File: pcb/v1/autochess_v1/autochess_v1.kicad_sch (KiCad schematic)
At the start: 3 parts, among them J1 Raspberry_Pi_2_3, U1 ATmega328P-P

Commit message: Make some progress on the PCB
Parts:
- added C65: 100uF, symbol Device:C
- added C66: 0.1uF, symbol Device:C
- added D65: 3A, symbol Device:D
- added F1: Polyfuse, symbol Device:Polyfuse
- added J2: POWER_IN, symbol Connector:Barrel_Jack
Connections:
- net GND: now also J1.14 (GND), J1.20 (GND), J1.25 (GND), J1.30 (GND), J1.34 (GND), J1.39 (GND), J1.6 (GND), J1.9 (GND), C65.2, C66.2, D65.2 (A), J2.2
- net VCC: now also J1.2 (5V), J1.4 (5V), C65.1, C66.1, D65.1 (K), F1.2
- net sensors/SENSOR_OUT_8: now reaches U1.1 (~{RESET}/PC6)
- net sensors/SENSOR_ON_6: now reaches U1.11 (PD5)
- net sensors/SENSOR_ON_7: now reaches U1.12 (PD6)
- net sensors/SENSOR_ON_8: now reaches U1.13 (PD7)
- net sensors/SENSOR_ON_1: now reaches U1.2 (PD0)
- net sensors/SENSOR_OUT_1: now reaches U1.23 (PC0)
- net sensors/SENSOR_OUT_2: now reaches U1.24 (PC1)
- net sensors/SENSOR_OUT_3: now reaches U1.25 (PC2)
- net sensors/SENSOR_OUT_4: now reaches U1.26 (PC3)
- net sensors/SENSOR_OUT_5: now reaches U1.27 (PC4)
- net sensors/SENSOR_OUT_6: now reaches U1.28 (PC5)
- net sensors/SENSOR_ON_2: now reaches U1.3 (PD1)
- net sensors/SENSOR_ON_3: now reaches U1.4 (PD2)
- net sensors/SENSOR_ON_4: now reaches U1.5 (PD3)
- net sensors/SENSOR_ON_5: now reaches U1.6 (PD4)
- new net: F1.1, J2.1
- no-connect marks 0 -> 4
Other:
- added sheet sensors (sensors.kicad_sch)
- note added: "TODO: Calculate fuse and TVS diode values"
- moved on the sheet: J1, R1, U1

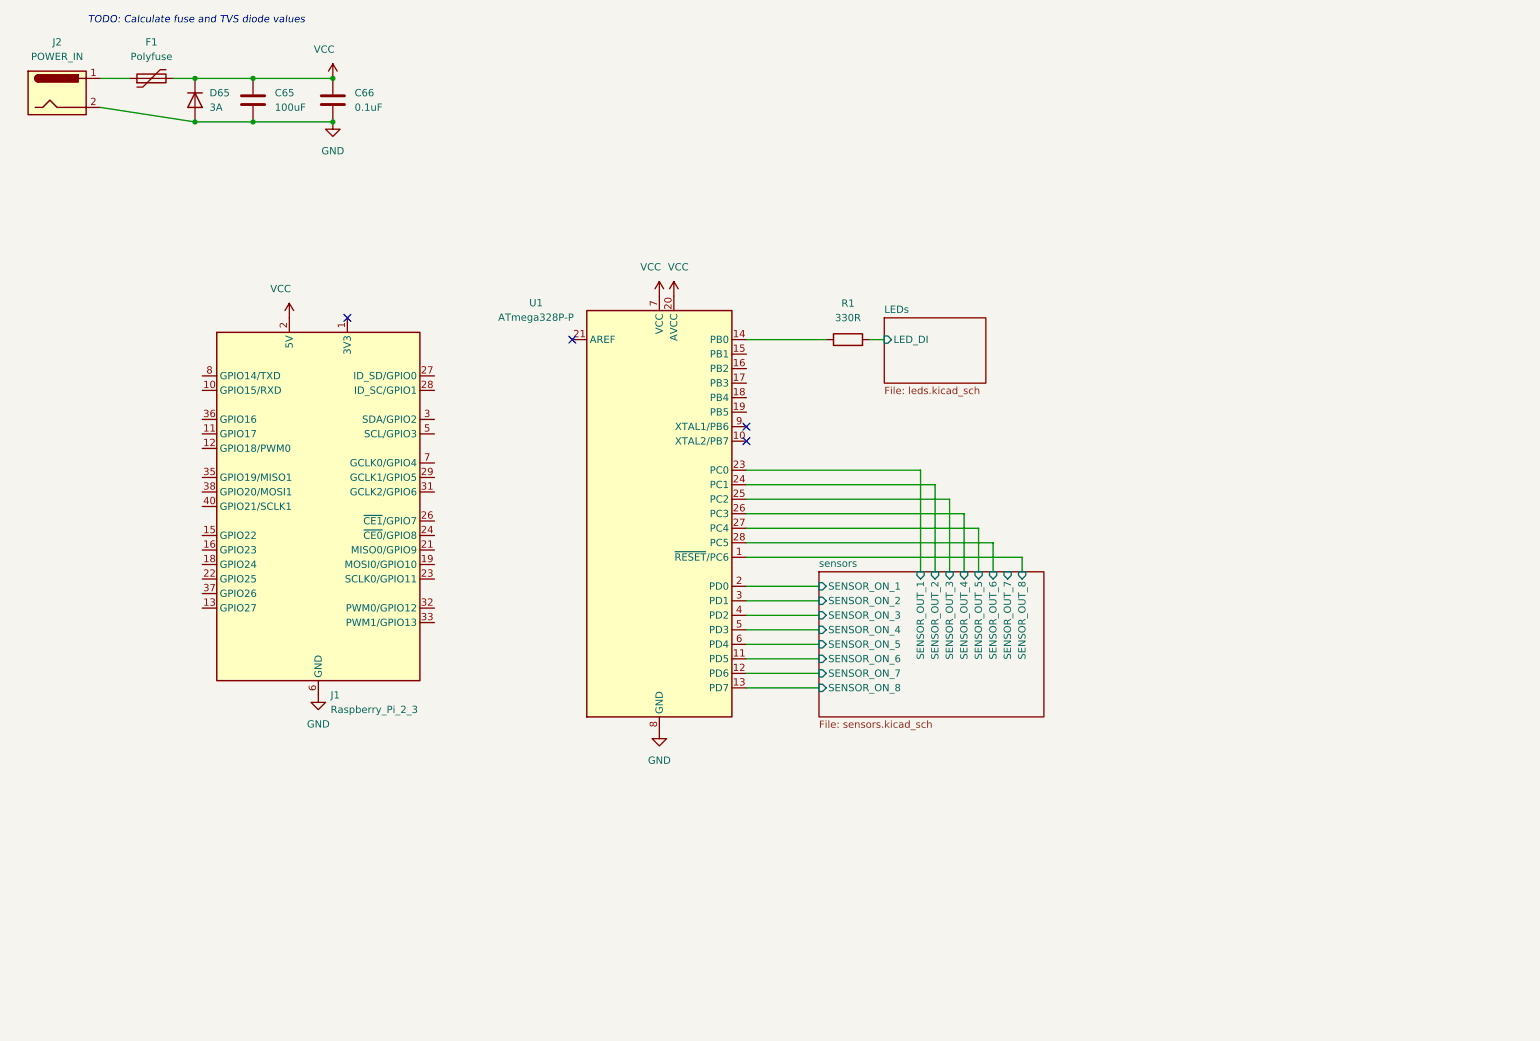
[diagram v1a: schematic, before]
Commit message: Finish the schematic draft, start pcb layout
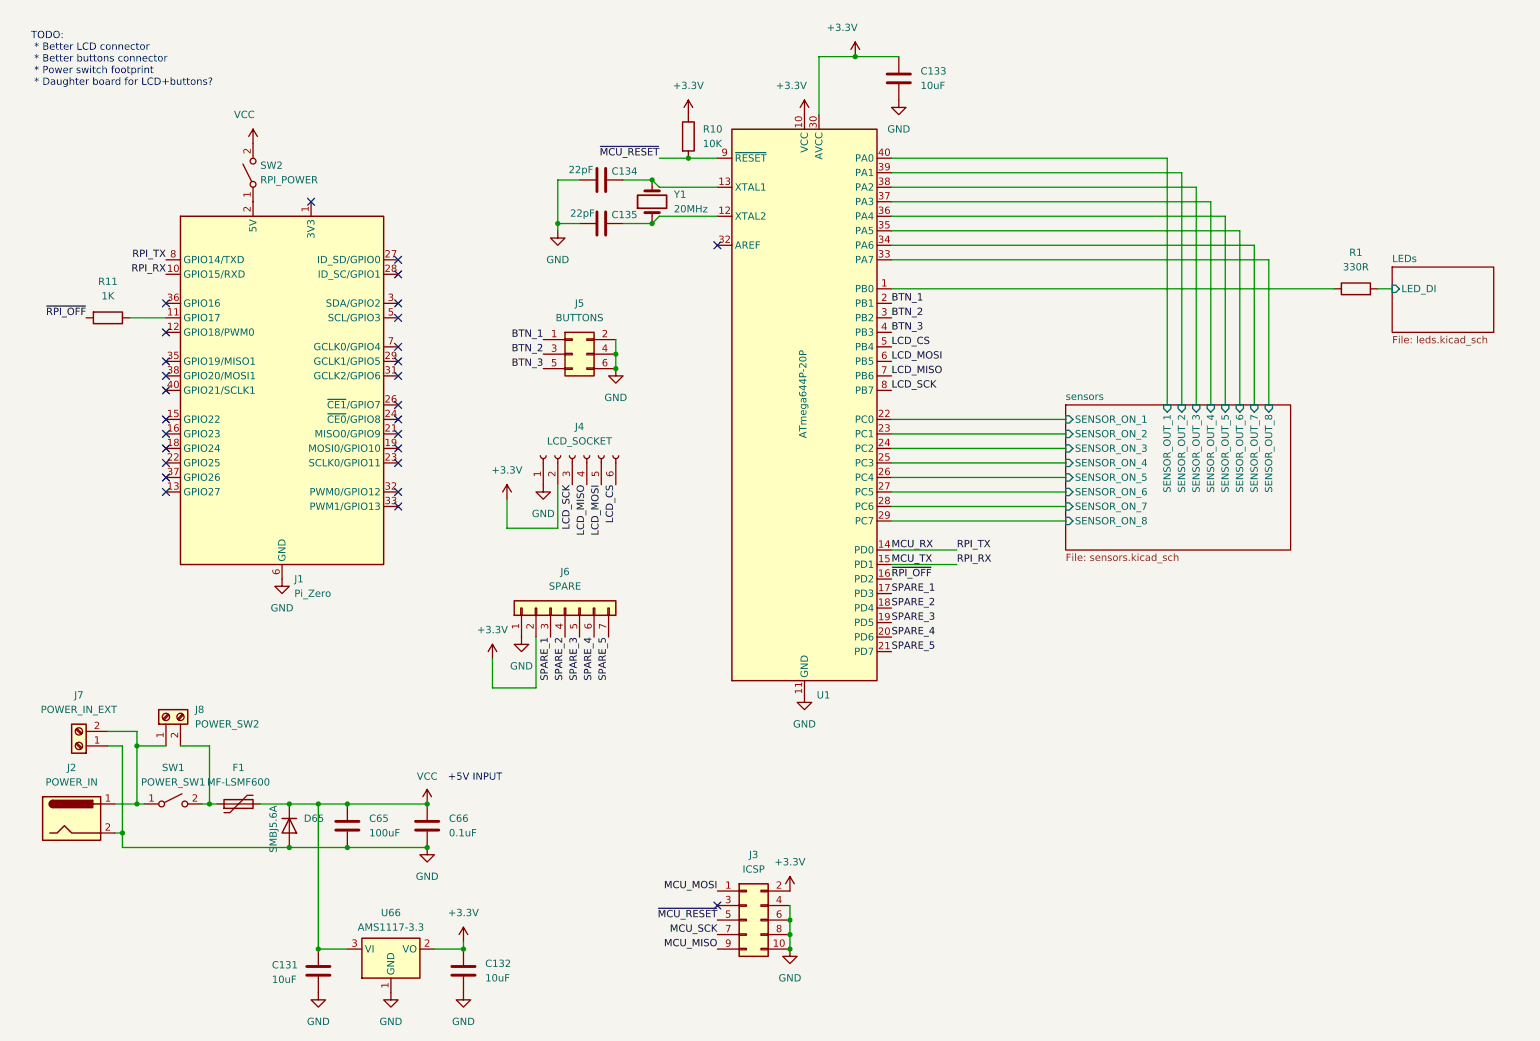
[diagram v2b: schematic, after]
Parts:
- removed U1: ATmega328P-P, Package_DIP:DIP-28_W7.62mm, symbol MCU_Microchip_ATmega:ATmega328P-P
- added C131, C132, C133: 10uF, Capacitor_SMD:C_1206_3216Metric_Pad1.33x1.80mm_HandSolder, symbol Device:C
- added C134, C135: 22pF, Capacitor_SMD:C_1206_3216Metric_Pad1.33x1.80mm_HandSolder, symbol Device:C
- added J3: ICSP, Connector_IDC:IDC-Header_2x05_P2.54mm_Horizontal, symbol Connector_Generic:Conn_02x05_Odd_Even
- added J4: LCD_SOCKET, Connector_PinHeader_2.54mm:PinHeader_1x06_P2.54mm_Vertical, symbol Connector:Conn_01x06_Socket
- added J5: BUTTONS, Connector_PinHeader_2.54mm:PinHeader_2x03_P2.54mm_Vertical, symbol Connector_Generic:Conn_02x03_Odd_Even
- added J6: SPARE, Connector_PinHeader_2.54mm:PinHeader_1x07_P2.54mm_Vertical, symbol Connector_Generic:Conn_01x07
- added J7: POWER_IN_EXT, TerminalBlock_Altech:Altech_AK100_1x02_P5.00mm, symbol Connector:Screw_Terminal_01x02
- added J8: POWER_SW2, TerminalBlock_Altech:Altech_AK100_1x02_P5.00mm, symbol Connector:Screw_Terminal_01x02
- added R10: 10K, Resistor_SMD:R_1206_3216Metric_Pad1.30x1.75mm_HandSolder, symbol Device:R
- added R11: 1K, Resistor_SMD:R_1206_3216Metric_Pad1.30x1.75mm_HandSolder, symbol Device:R
- added SW1: POWER_SW1, Autochess:Marquardt_1858_4205, symbol Switch:SW_SPST
- added SW2: RPI_POWER, Jumper:SolderJumper-2_P1.3mm_Open_TrianglePad1.0x1.5mm, symbol Switch:SW_SPST
- added U1: ATmega644P-20P, Package_DIP:DIP-40_W15.24mm, symbol MCU_Microchip_ATmega:ATmega644P-20P
- added U66: AMS1117-3.3, Package_TO_SOT_SMD:SOT-223-3_TabPin2, symbol Regulator_Linear:AMS1117-3.3
- added Y1: 20MHz, Crystal:Crystal_HC49-U_Vertical, symbol Device:Crystal
- C65, C66: footprint (none) -> Capacitor_SMD:C_1206_3216Metric_Pad1.33x1.80mm_HandSolder
- D65: value 3A -> SMBJ5.6A; footprint (none) -> Diode_SMD:D_SMB_Handsoldering
- F1: value Polyfuse -> MF-LSMF600; footprint (none) -> Fuse:Fuse_2920_7451Metric_Pad2.10x5.45mm_HandSolder
- J1: value Raspberry_Pi_2_3 -> Pi_Zero; footprint (none) -> Connector_PinHeader_2.54mm:PinHeader_2x20_P2.54mm_Vertical
- J2: footprint (none) -> Connector_BarrelJack:BarrelJack_Horizontal
- R1: footprint (none) -> Resistor_SMD:R_1206_3216Metric_Pad1.30x1.75mm_HandSolder
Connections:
- net GND: now also C131.2, C132.2, C133.2, C134.2, C135.2, J3.10 (Pin_10), J3.4 (Pin_4), J3.6 (Pin_6), J3.8 (Pin_8), J4.1 (Pin_1), J5.2 (Pin_2), J5.4 (Pin_4), J5.6 (Pin_6), J6.1 (Pin_1), J7.1 (Pin_1), U1.11 (GND), U1.31 (GND), U66.1 (GND)
- net VCC: now also C131.1, SW2.2 (B), U66.3 (VI); no longer J1.2 (5V), J1.4 (5V)
- net sensors/SENSOR_ON_1: now also U1.22 (PC0)
- net sensors/SENSOR_ON_2: now also U1.23 (PC1)
- net sensors/SENSOR_ON_3: now also U1.24 (PC2)
- net sensors/SENSOR_ON_4: now also U1.25 (PC3)
- net sensors/SENSOR_ON_5: now also U1.26 (PC4)
- net sensors/SENSOR_ON_6: now also U1.27 (PC5)
- net sensors/SENSOR_ON_7: now also U1.28 (PC6)
- net sensors/SENSOR_ON_8: now also U1.29 (PC7)
- net sensors/SENSOR_OUT_1: now also U1.40 (PA0)
- net sensors/SENSOR_OUT_2: now also U1.39 (PA1)
- net sensors/SENSOR_OUT_3: now also U1.38 (PA2)
- net sensors/SENSOR_OUT_4: now also U1.37 (PA3)
- net sensors/SENSOR_OUT_5: now also U1.36 (PA4)
- net sensors/SENSOR_OUT_6: now also U1.35 (PA5)
- net sensors/SENSOR_OUT_7: now also U1.34 (PA6)
- net sensors/SENSOR_OUT_8: now also U1.33 (PA7)
- net MCU_TX: now reaches J1.10 (GPIO15/RXD)
- net MCU_TX: now also U1.15 (PD1)
- net at J1.11 (GPIO17): now also R11.1
- net MCU_RX: now reaches J1.8 (GPIO14/TXD)
- net MCU_RX: now also U1.14 (PD0)
- net at R1.1: now also U1.1 (PB0)
- net at J2.1: now also J7.2 (Pin_2), J8.1 (Pin_1), SW1.1 (A); no longer F1.1
- new net: J1.2 (5V), J1.4 (5V), SW2.1 (A)
- new net: F1.1, J8.2 (Pin_2), SW1.2 (B)
- new net: C135.1, U1.12 (XTAL2), Y1.1
- new net: C134.1, U1.13 (XTAL1), Y1.2
- new net +3.3V: C132.1, C133.1, J3.2 (Pin_2), J4.2 (Pin_2), J6.2 (Pin_2), R10.1, U1.10 (VCC), U1.30 (AVCC), U66.2 (VO)
- new net BTN_1: J5.1 (Pin_1), U1.2 (PB1)
- new net BTN_2: J5.3 (Pin_3), U1.3 (PB2)
- new net BTN_3: J5.5 (Pin_5), U1.4 (PB3)
- new net LCD_CS: J4.6 (Pin_6), U1.5 (PB4)
- new net LCD_MISO: J4.4 (Pin_4), U1.7 (PB6)
- new net LCD_MOSI: J4.5 (Pin_5), U1.6 (PB5)
- new net LCD_SCK: J4.3 (Pin_3), U1.8 (PB7)
- new net MCU_MISO: J3.9 (Pin_9)
- new net MCU_MOSI: J3.1 (Pin_1)
- new net MCU_SCK: J3.7 (Pin_7)
- new net SPARE_1: J6.3 (Pin_3), U1.17 (PD3)
- new net SPARE_2: J6.4 (Pin_4), U1.18 (PD4)
- new net SPARE_3: J6.5 (Pin_5), U1.19 (PD5)
- new net SPARE_4: J6.6 (Pin_6), U1.20 (PD6)
- new net SPARE_5: J6.7 (Pin_7), U1.21 (PD7)
- new net ~{MCU_RESET}: J3.5 (Pin_5), R10.2, U1.9 (~{RESET})
- new net ~{RPI_OFF}: R11.2, U1.16 (PD2)
- no-connect marks 4 -> 28
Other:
- note added: "+5V INPUT"
- note added: "TODO: * Better LCD connector * Better buttons connector * Power switch footprint * Daughter board for LCD+buttons?"
- note removed: "TODO: Calculate fuse and TVS diode values"
- moved on the sheet: C65, C66, D65, F1, J1, J2, R1

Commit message: Continue laying out the PCB
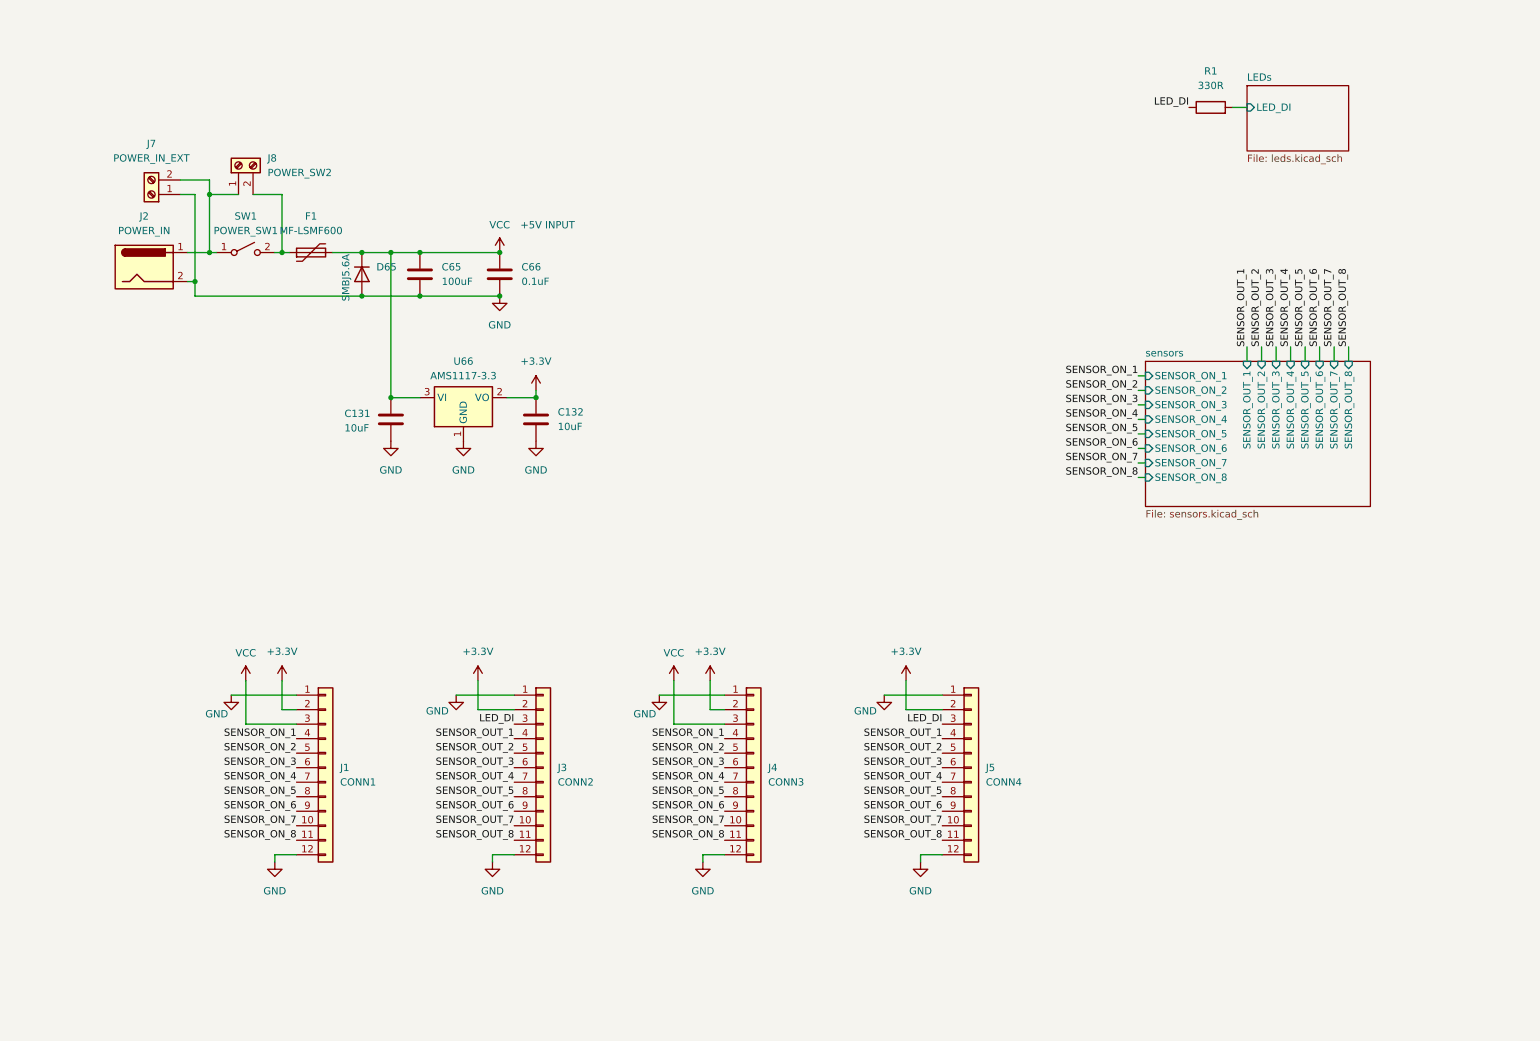
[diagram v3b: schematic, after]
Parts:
- removed C133: 10uF, Capacitor_SMD:C_1206_3216Metric_Pad1.33x1.80mm_HandSolder, symbol Device:C
- removed C134, C135: 22pF, Capacitor_SMD:C_1206_3216Metric_Pad1.33x1.80mm_HandSolder, symbol Device:C
- removed J1: Pi_Zero, Connector_PinHeader_2.54mm:PinHeader_2x20_P2.54mm_Vertical, symbol Connector:Raspberry_Pi_2_3
- removed J3: ICSP, Connector_IDC:IDC-Header_2x05_P2.54mm_Horizontal, symbol Connector_Generic:Conn_02x05_Odd_Even
- removed J4: LCD_SOCKET, Connector_PinHeader_2.54mm:PinHeader_1x06_P2.54mm_Vertical, symbol Connector:Conn_01x06_Socket
- removed J5: BUTTONS, Connector_PinHeader_2.54mm:PinHeader_2x03_P2.54mm_Vertical, symbol Connector_Generic:Conn_02x03_Odd_Even
- removed J6: SPARE, Connector_PinHeader_2.54mm:PinHeader_1x07_P2.54mm_Vertical, symbol Connector_Generic:Conn_01x07
- removed R10: 10K, Resistor_SMD:R_1206_3216Metric_Pad1.30x1.75mm_HandSolder, symbol Device:R
- removed R11: 1K, Resistor_SMD:R_1206_3216Metric_Pad1.30x1.75mm_HandSolder, symbol Device:R
- removed SW2: RPI_POWER, Jumper:SolderJumper-2_P1.3mm_Open_TrianglePad1.0x1.5mm, symbol Switch:SW_SPST
- removed U1: ATmega644P-20P, Package_DIP:DIP-40_W15.24mm, symbol MCU_Microchip_ATmega:ATmega644P-20P
- removed Y1: 20MHz, Crystal:Crystal_HC49-U_Vertical, symbol Device:Crystal
- added J1: CONN1, Connector_PinHeader_2.54mm:PinHeader_1x12_P2.54mm_Vertical, symbol Connector_Generic:Conn_01x12
- added J3: CONN2, Connector_PinHeader_2.54mm:PinHeader_1x12_P2.54mm_Vertical, symbol Connector_Generic:Conn_01x12
- added J4: CONN3, Connector_PinHeader_2.54mm:PinHeader_1x12_P2.54mm_Vertical, symbol Connector_Generic:Conn_01x12
- added J5: CONN4, Connector_PinHeader_2.54mm:PinHeader_1x12_P2.54mm_Vertical, symbol Connector_Generic:Conn_01x12
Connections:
- net +3.3V: now also J1.2 (Pin_2), J3.2 (Pin_2), J4.2 (Pin_2), J5.2 (Pin_2)
- net GND: now also J1.1 (Pin_1), J1.12 (Pin_12), J3.1 (Pin_1), J3.12 (Pin_12), J4.1 (Pin_1), J4.12 (Pin_12), J5.1 (Pin_1), J5.12 (Pin_12)
- net VCC: now also J1.3 (Pin_3), J4.3 (Pin_3)
- net LED_DI: now reaches R1.1
- net LED_DI: now also J3.3 (Pin_3), J5.3 (Pin_3)
- new net SENSOR_ON_1: J1.4 (Pin_4), J4.4 (Pin_4)
- new net SENSOR_ON_2: J1.5 (Pin_5), J4.5 (Pin_5)
- new net SENSOR_ON_3: J1.6 (Pin_6), J4.6 (Pin_6)
- new net SENSOR_ON_4: J1.7 (Pin_7), J4.7 (Pin_7)
- new net SENSOR_ON_5: J1.8 (Pin_8), J4.8 (Pin_8)
- new net SENSOR_ON_6: J1.9 (Pin_9), J4.9 (Pin_9)
- new net SENSOR_ON_7: J1.10 (Pin_10), J4.10 (Pin_10)
- new net SENSOR_ON_8: J1.11 (Pin_11), J4.11 (Pin_11)
- new net SENSOR_OUT_1: J3.4 (Pin_4), J5.4 (Pin_4)
- new net SENSOR_OUT_2: J3.5 (Pin_5), J5.5 (Pin_5)
- new net SENSOR_OUT_3: J3.6 (Pin_6), J5.6 (Pin_6)
- new net SENSOR_OUT_4: J3.7 (Pin_7), J5.7 (Pin_7)
- new net SENSOR_OUT_5: J3.8 (Pin_8), J5.8 (Pin_8)
- new net SENSOR_OUT_6: J3.9 (Pin_9), J5.9 (Pin_9)
- new net SENSOR_OUT_7: J3.10 (Pin_10), J5.10 (Pin_10)
- new net SENSOR_OUT_8: J3.11 (Pin_11), J5.11 (Pin_11)
- no-connect marks 28 -> 0
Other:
- note removed: "TODO: * Better LCD connector * Better buttons connector * Power switch footprint * Daughter board for LCD+buttons?"
- moved on the sheet: C131, C132, C65, C66, D65, F1, J2, J7, J8, R1, SW1, U66

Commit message: Continue placing
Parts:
- renumbered C65 to C133, C66 to C134
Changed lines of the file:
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@@
 		(dnp no)
 		(fields_autoplaced yes)
-		(property "Reference" "C66"
+		(property "Reference" "C134"
 			(at 102.87 59.6899 0)
 			(show_name no)
@@
 			(project "autochess_v1"
 				(path "/3df8ff08-9f77-4f65-9fed-81b599c9e86e"
-					(reference "C66")
+					(reference "C134")
 					(unit 1)
 				)
@@
 		(dnp no)
 		(fields_autoplaced yes)
-		(property "Reference" "C65"
+		(property "Reference" "C133"
 			(at 88.9 59.6899 0)
 			(show_name no)
@@
 			(project "autochess_v1"
 				(path "/3df8ff08-9f77-4f65-9fed-81b599c9e86e"
-					(reference "C65")
+					(reference "C133")
 					(unit 1)
 				)

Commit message: Place most components
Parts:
- renumbered J3 to J2, J4 to J3, J5 to J4, J2 to J9
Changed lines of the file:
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@@
 		(dnp no)
 		(fields_autoplaced yes)
-		(property "Reference" "J3"
+		(property "Reference" "J2"
 			(at 109.22 147.3199 0)
 			(show_name no)
@@
 			(project "autochess_v1"
 				(path "/3df8ff08-9f77-4f65-9fed-81b599c9e86e"
-					(reference "J3")
+					(reference "J2")
 					(unit 1)
 				)
@@
 		(dnp no)
 		(fields_autoplaced yes)
-		(property "Reference" "J2"
+		(property "Reference" "J9"
 			(at 36.83 50.8 0)
 			(show_name no)
@@
 			(project "autochess_v1"
 				(path "/3df8ff08-9f77-4f65-9fed-81b599c9e86e"
-					(reference "J2")
+					(reference "J9")
 					(unit 1)
 				)
@@
 		(dnp no)
 		(fields_autoplaced yes)
-		(property "Reference" "J5"
+		(property "Reference" "J4"
 			(at 184.15 147.3199 0)
 			(show_name no)
@@
 			(project "autochess_v1"
 				(path "/3df8ff08-9f77-4f65-9fed-81b599c9e86e"
-					(reference "J5")
+					(reference "J4")
 					(unit 1)
 				)
@@
 		(dnp no)
 		(fields_autoplaced yes)
-		(property "Reference" "J4"
+		(property "Reference" "J3"
 			(at 146.05 147.3199 0)
 			(show_name no)
@@
 			(project "autochess_v1"
 				(path "/3df8ff08-9f77-4f65-9fed-81b599c9e86e"
-					(reference "J4")
-					(unit 1)
-				)
+					(reference "J3")
+					(unit 1)
+				)

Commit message: Continue PCB layout
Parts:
- removed J7: POWER_IN_EXT, TerminalBlock_Altech:Altech_AK100_1x02_P5.00mm, symbol Connector:Screw_Terminal_01x02
- removed J8: POWER_SW2, TerminalBlock_Altech:Altech_AK100_1x02_P5.00mm, symbol Connector:Screw_Terminal_01x02
